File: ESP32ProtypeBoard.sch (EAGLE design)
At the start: 100 parts, among them IC1 SOIC-8, IC2 SI4431BDY, J10 POWER_JACKPTH_LOCK, Q2 MMBT3904, Q3 MMBT3904, U2 ESP-WROOM-32

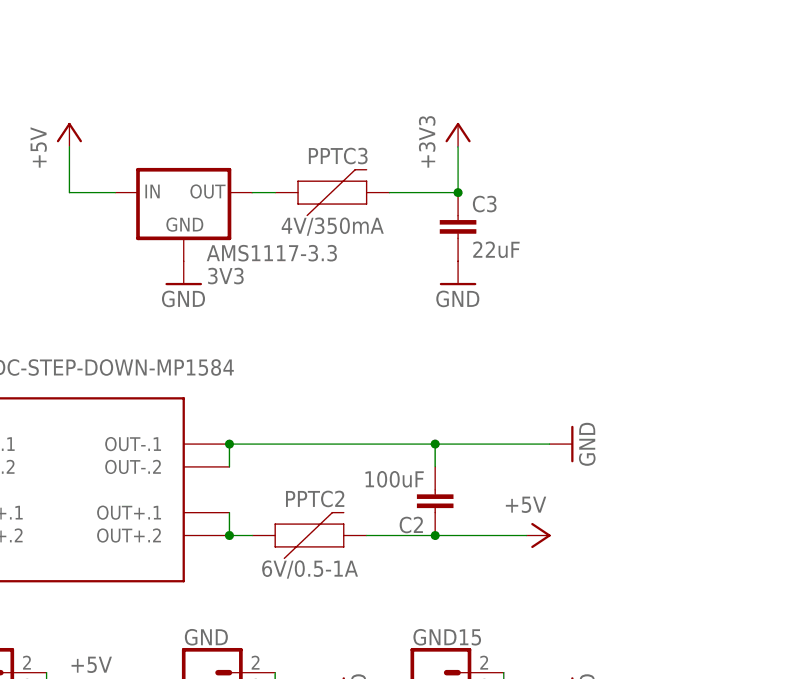
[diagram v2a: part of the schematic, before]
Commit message: Moved REG close to ESP to allow very small cutout
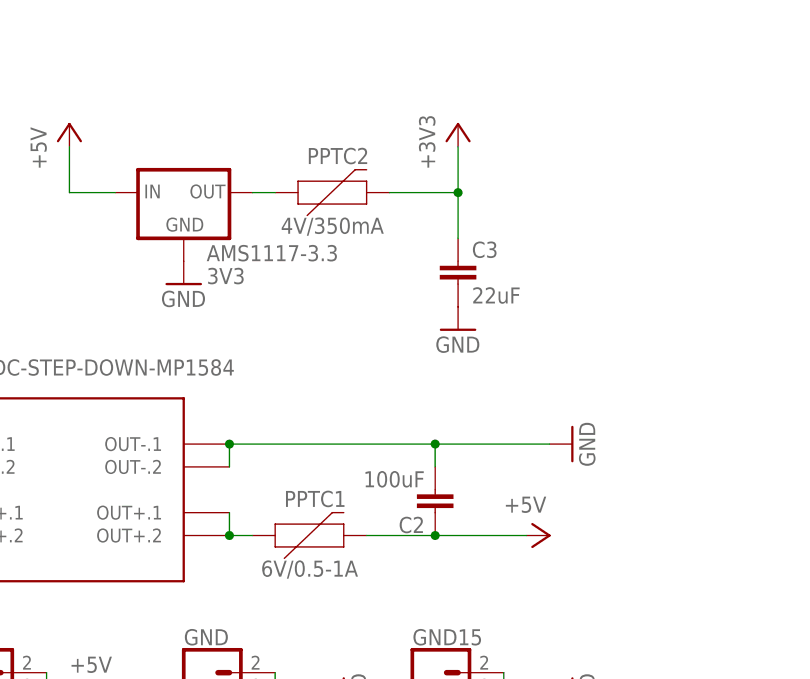
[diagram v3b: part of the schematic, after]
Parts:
- removed PPTC3: 4V/350mA, SparkFun-Fuses:PPTC_THREE-QUARTER-AMP
- added PPTC1: 6V/0.5-1A, SparkFun-Fuses:PPTC_THREE-QUARTER-AMP
- PPTC2: value 6V/0.5-1A -> 4V/350mA
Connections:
- net +3V3: now also PPTC2.2; no longer PPTC3.2
- net +5V: now also PPTC1.2; no longer PPTC2.2
- net 3V3OUT: now also PPTC2.1; no longer PPTC3.1
- net 5VOUT: now also PPTC1.1; no longer PPTC2.1
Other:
- moved on the sheet: C3, PPTC2
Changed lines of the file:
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@@
 <part name="+3V2" library="supply1" library_urn="urn:adsk.eagle:library:371" deviceset="+3V3" device=""/>
 <part name="P+11" library="supply1" library_urn="urn:adsk.eagle:library:371" deviceset="VCC" device=""/>
-<part name="PPTC2" library="SparkFun-Fuses" deviceset="PPTC" device="_THREE-QUARTER-AMP" value="6V/0.5-1A"/>
-<part name="PPTC3" library="SparkFun-Fuses" deviceset="PPTC" device="_THREE-QUARTER-AMP" value="4V/350mA"/>
+<part name="PPTC1" library="SparkFun-Fuses" deviceset="PPTC" device="_THREE-QUARTER-AMP" value="6V/0.5-1A"/>
+<part name="PPTC2" library="SparkFun-Fuses" deviceset="PPTC" device="_THREE-QUARTER-AMP" value="4V/350mA"/>
 <part name="+3V10" library="supply1" library_urn="urn:adsk.eagle:library:371" deviceset="+3V3" device=""/>
 <part name="GND4" library="supply1" library_urn="urn:adsk.eagle:library:371" deviceset="GND" device=""/>
@@
 <attribute name="VALUE" x="38.1" y="81.28" size="1.778" layer="96" rot="R90"/>
 </instance>
-<instance part="C3" gate="G$1" x="106.68" y="88.9" smashed="yes">
-<attribute name="NAME" x="108.204" y="89.281" size="1.778" layer="95"/>
-<attribute name="VALUE" x="108.204" y="84.201" size="1.778" layer="96"/>
-</instance>
-<instance part="GND13" gate="1" x="106.68" y="81.28" smashed="yes">
-<attribute name="VALUE" x="104.14" y="78.74" size="1.778" layer="96"/>
+<instance part="C3" gate="G$1" x="106.68" y="83.82" smashed="yes">
+<attribute name="NAME" x="108.204" y="84.201" size="1.778" layer="95"/>
+<attribute name="VALUE" x="108.204" y="79.121" size="1.778" layer="96"/>
+</instance>
+<instance part="GND13" gate="1" x="106.68" y="76.2" smashed="yes">
+<attribute name="VALUE" x="104.14" y="73.66" size="1.778" layer="96"/>
 </instance>
 <instance part="+5V" gate="G$1" x="53.34" y="35.56" smashed="yes">
@@
 <attribute name="VALUE" x="22.86" y="15.24" size="1.778" layer="96" rot="R180"/>
 </instance>
-<instance part="PPTC2" gate="F1" x="88.9" y="53.34" smashed="yes">
+<instance part="PPTC1" gate="F1" x="88.9" y="53.34" smashed="yes">
 <attribute name="NAME" x="90.805" y="56.515" size="1.778" layer="95" font="vector" align="bottom-center"/>
 <attribute name="VALUE" x="90.17" y="50.546" size="1.778" layer="96" font="vector" align="top-center"/>
 </instance>
-<instance part="PPTC3" gate="F1" x="91.44" y="91.44" smashed="yes">
+<instance part="PPTC2" gate="F1" x="91.44" y="91.44" smashed="yes">
 <attribute name="NAME" x="93.345" y="94.615" size="1.778" layer="95" font="vector" align="bottom-center"/>
 <attribute name="VALUE" x="92.71" y="88.646" size="1.778" layer="96" font="vector" align="top-center"/>
@@
 <segment>
 <pinref part="+3V4" gate="G$1" pin="+3V3"/>
+<wire x1="106.68" y1="91.44" x2="106.68" y2="96.52" width="0.1524" layer="91"/>
+<pinref part="PPTC2" gate="F1" pin="2"/>
+<wire x1="99.06" y1="91.44" x2="106.68" y2="91.44" width="0.1524" layer="91"/>
 <pinref part="C3" gate="G$1" pin="1"/>
-<wire x1="106.68" y1="91.44" x2="106.68" y2="96.52" width="0.1524" layer="91"/>
+<wire x1="106.68" y1="86.36" x2="106.68" y2="91.44" width="0.1524" layer="91"/>
 <junction x="106.68" y="91.44"/>
-<wire x1="99.06" y1="91.44" x2="106.68" y2="91.44" width="0.1524" layer="91"/>
-<pinref part="PPTC3" gate="F1" pin="2"/>
 </segment>
 <segment>
@@
 <pinref part="P+1" gate="1" pin="+5V"/>
 <wire x1="96.52" y1="53.34" x2="104.14" y2="53.34" width="0.1524" layer="91"/>
-<pinref part="PPTC2" gate="F1" pin="2"/>
+<pinref part="PPTC1" gate="F1" pin="2"/>
 </segment>
 <segment>
@@
 <net name="5VOUT" class="0">
 <segment>
-<pinref part="PPTC2" gate="F1" pin="1"/>
+<pinref part="PPTC1" gate="F1" pin="1"/>
 <pinref part="U$2" gate="G$1" pin="OUT+.2"/>
 <pinref part="U$2" gate="G$1" pin="OUT+.1"/>
@@
 <pinref part="AMS1117-3.3" gate="G$1" pin="OUT"/>
 <wire x1="83.82" y1="91.44" x2="86.36" y2="91.44" width="0.1524" layer="91"/>
-<pinref part="PPTC3" gate="F1" pin="1"/>
-</segment>
-</net>
+<pinref part="PPTC2" gate="F1" pin="1"/>
+</segment>
+</net>

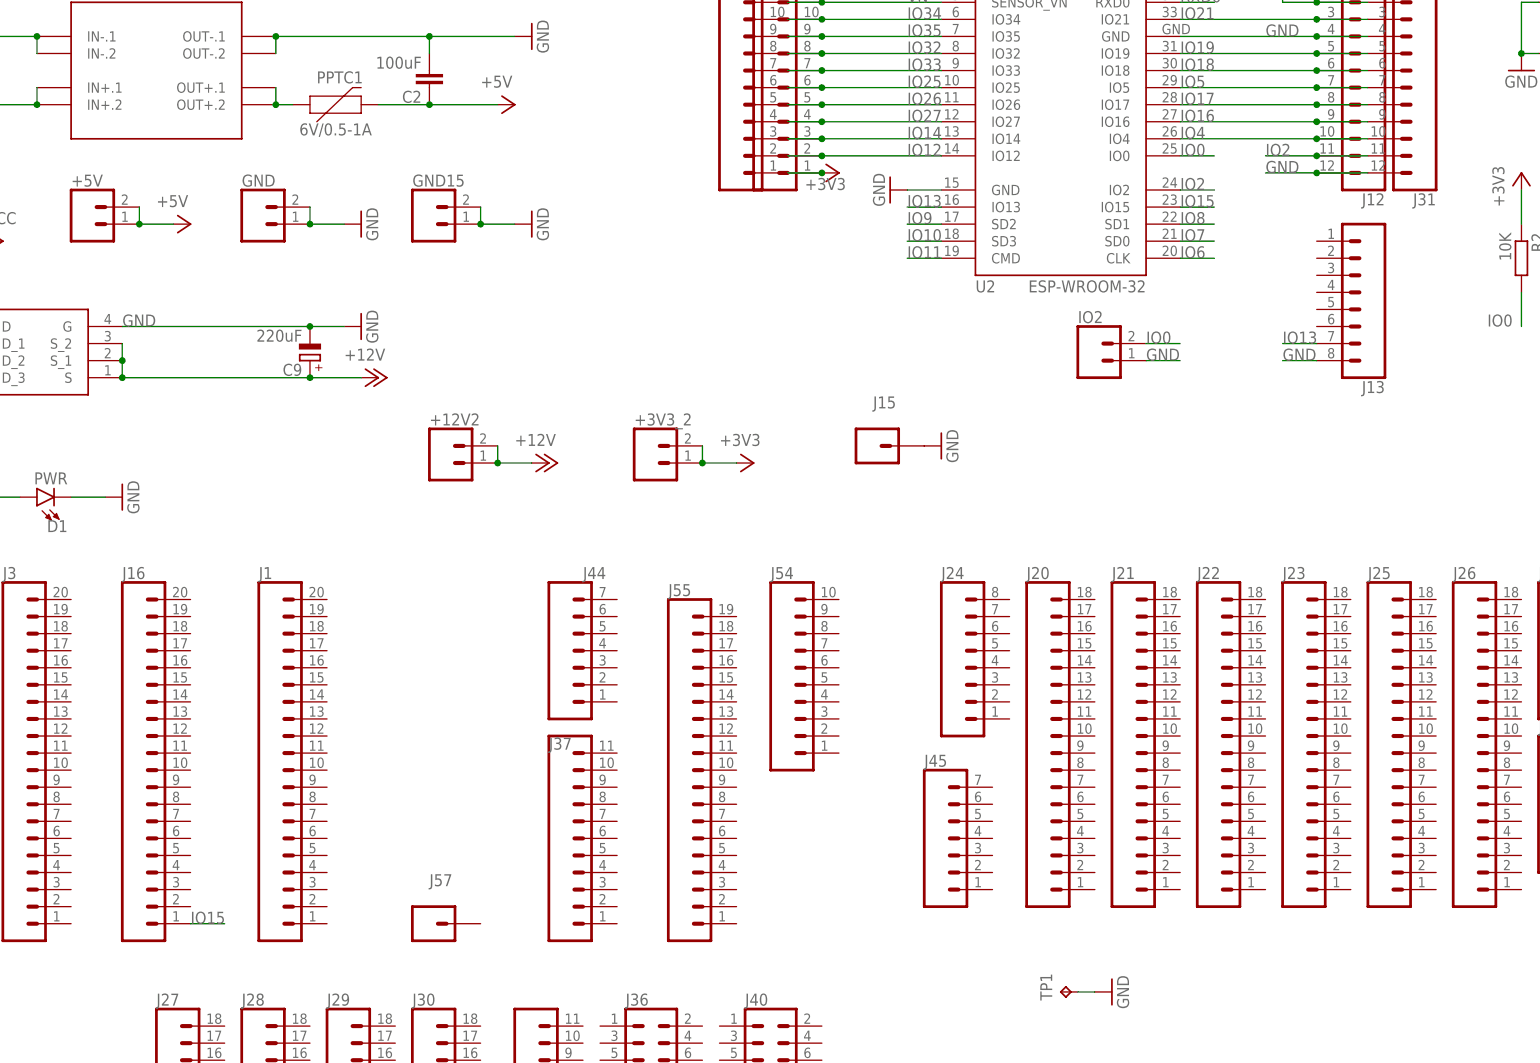
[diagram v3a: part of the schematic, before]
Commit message: Rewired pins under ESP etc
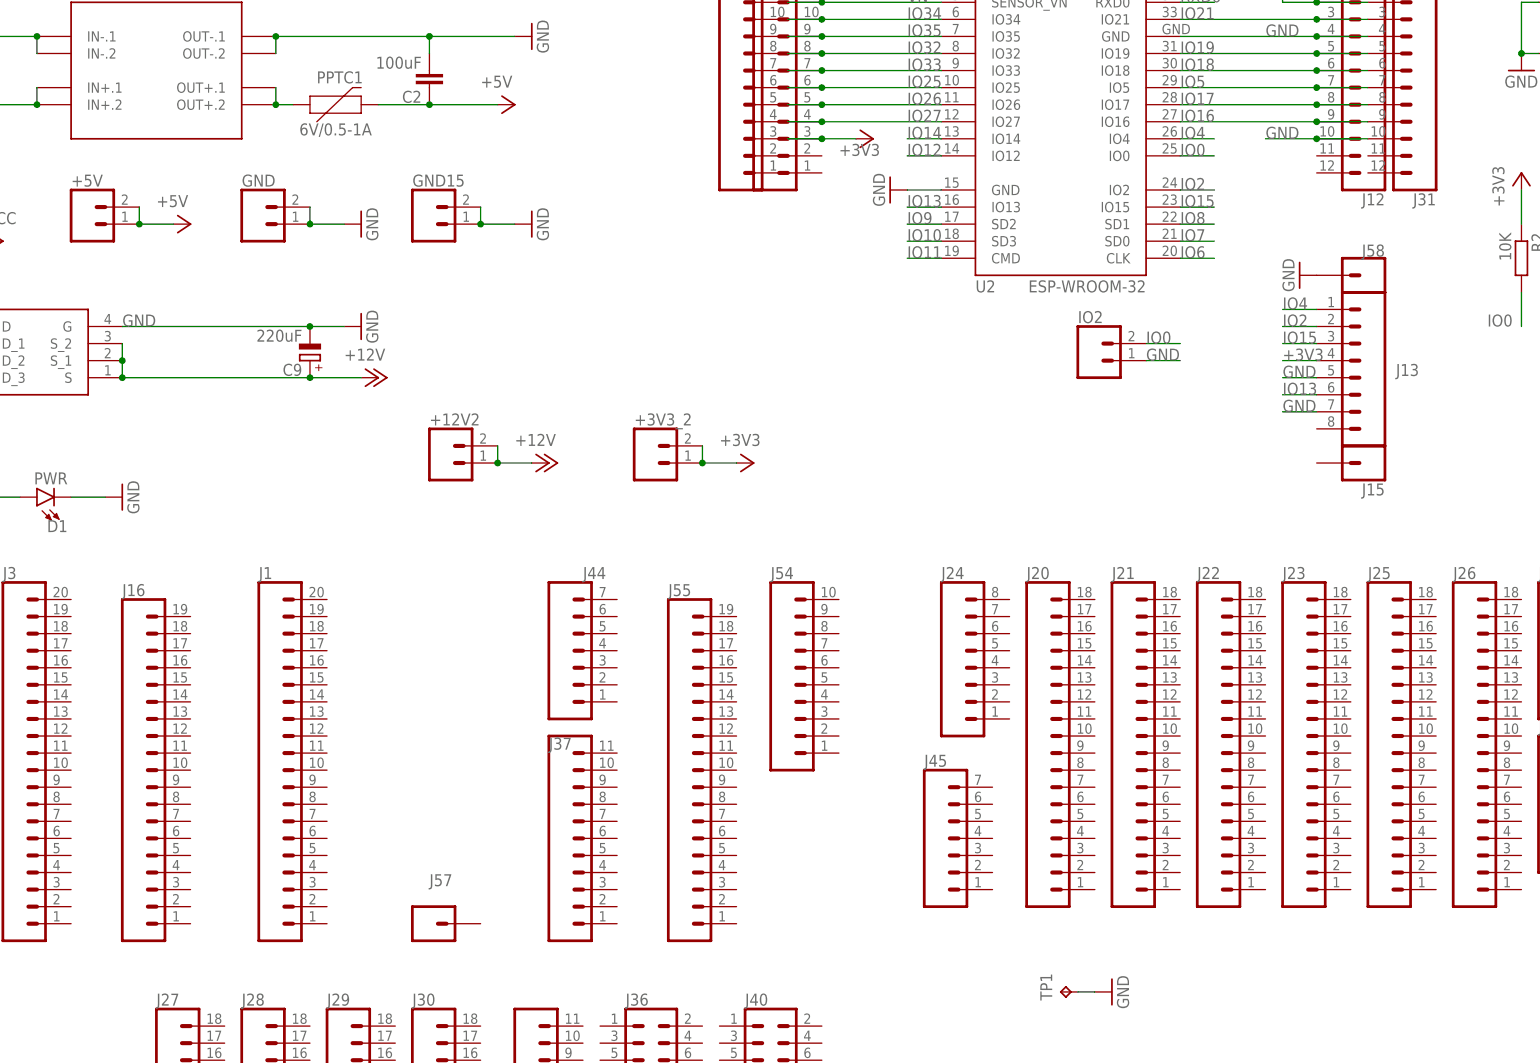
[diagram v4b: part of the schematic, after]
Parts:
- added J58: (no value), SparkFun-Connectors:CONN_01PTH_NO_SILK_KIT
- J16: device SparkFun-Connectors:CONN_20NOSILK -> SparkFun-Connectors:CONN_191X19_NO_SILK
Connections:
- net +3V3: now also J11.3, J13.4, J14.3; no longer J11.1, J14.1
- net GND: now also J12.10, J13.5, J13.7, J31.10, J58.1; no longer J12.12, J13.8, J15.1, J31.12
- net IO12: no longer J11.2, J14.2
- net IO13: now also J13.6; no longer J13.7
- net IO14: no longer J11.3, J14.3
- net IO15: now also J13.3; no longer J16.1
- net IO2: now also J13.2; no longer J12.11, J31.11
- net IO4: now also J13.1; no longer J12.10, J31.10
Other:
- moved on the sheet: J13, J15

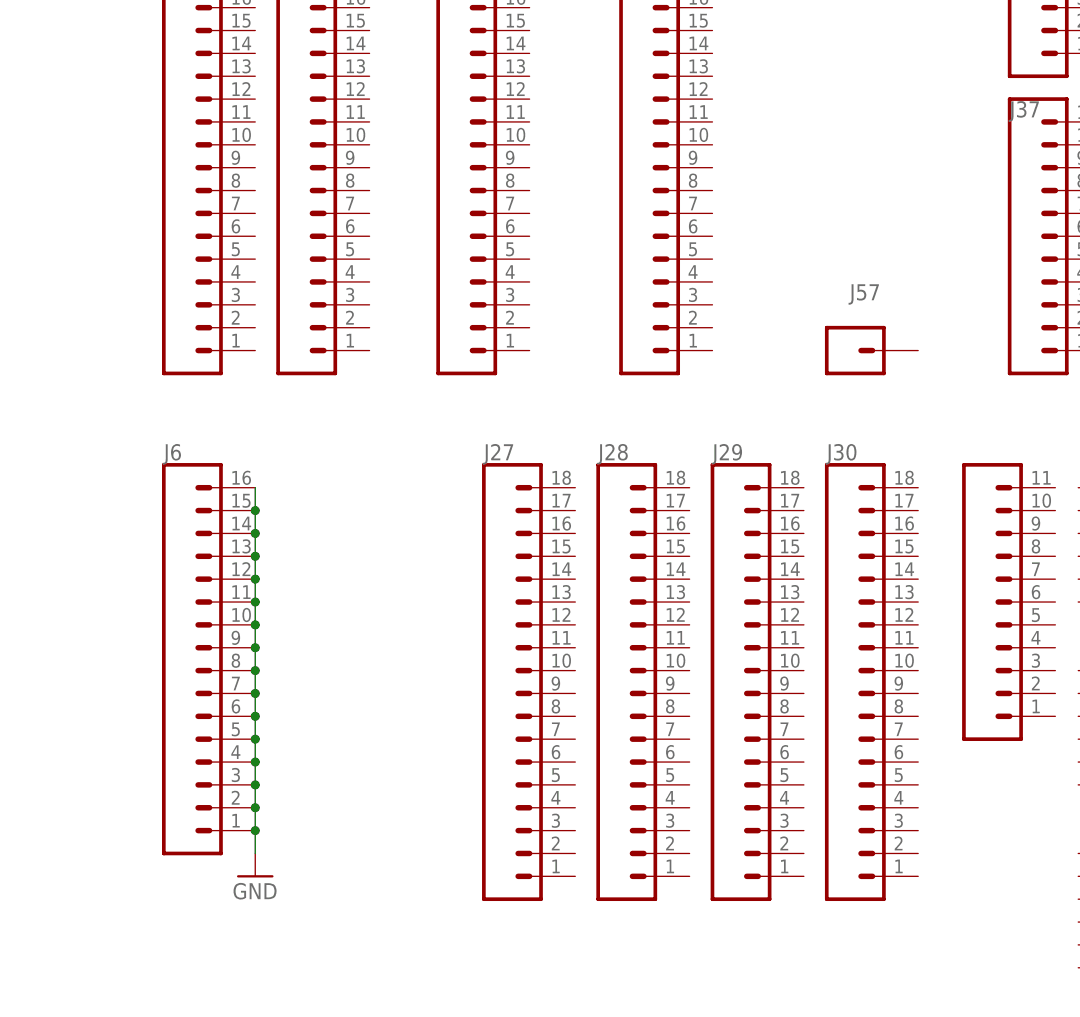
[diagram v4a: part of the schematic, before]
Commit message: Moving around power pins to save space
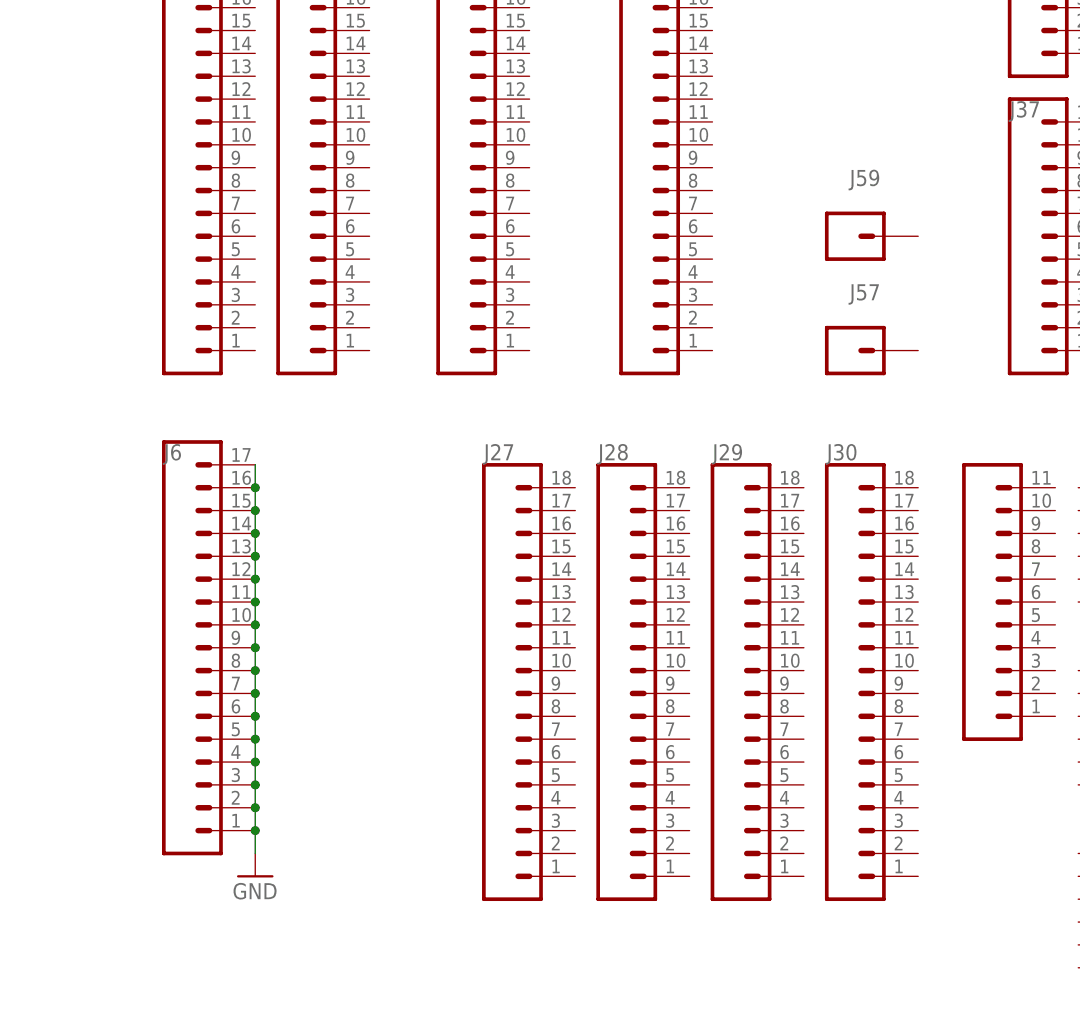
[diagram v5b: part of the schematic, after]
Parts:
- added J59: (no value), SparkFun-Connectors:CONN_01PTH_NO_SILK_KIT
- J6: device SparkFun-Connectors:CONN_161X16_NO_SILK -> SparkFun-Connectors:CONN_17NOSILK
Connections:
- net GND: now also J6.17
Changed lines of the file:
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@@
 <part name="J4" library="SparkFun-Connectors" library_urn="urn:adsk.eagle:library:513" deviceset="CONN_02" device="1X02_NO_SILK" package3d_urn="urn:adsk.eagle:package:38051/1"/>
 <part name="J5" library="SparkFun-Connectors" deviceset="CONN_16" device="1X16_NO_SILK"/>
-<part name="J6" library="SparkFun-Connectors" deviceset="CONN_16" device="1X16_NO_SILK"/>
+<part name="J6" library="SparkFun-Connectors" library_urn="urn:adsk.eagle:library:513" deviceset="CONN_17" device="NOSILK" package3d_urn="urn:adsk.eagle:package:38192/1"/>
 <part name="J7" library="SparkFun-Connectors" deviceset="CONN_06X2" device="NO_SILK"/>
 <part name="J8" library="SparkFun-Connectors" library_urn="urn:adsk.eagle:library:513" deviceset="CONN_11" device="1X11_NO_SILK" package3d_urn="urn:adsk.eagle:package:38260/1"/>
@@
 <part name="GND9" library="supply1" library_urn="urn:adsk.eagle:library:371" deviceset="GND" device=""/>
 <part name="+3V7" library="supply1" library_urn="urn:adsk.eagle:library:371" deviceset="+3V3" device=""/>
+<part name="J59" library="SparkFun-Connectors" library_urn="urn:adsk.eagle:library:513" deviceset="CONN_01" device="PTH_NO_SILK_KIT" package3d_urn="urn:adsk.eagle:package:38038/1"/>
 </parts>
 <sheets>
@@
 <instance part="+3V7" gate="G$1" x="170.18" y="48.26" smashed="yes" rot="R270">
 <attribute name="VALUE" x="165.1" y="45.72" size="1.778" layer="96"/>
+</instance>
+<instance part="J59" gate="G$1" x="104.14" y="-55.88" smashed="yes">
+<attribute name="VALUE" x="104.14" y="-55.626" size="1.778" layer="96" font="vector"/>
+<attribute name="NAME" x="104.14" y="-50.292" size="1.778" layer="95" font="vector"/>
 </instance>
 </instances>
@@
 <wire x1="38.1" y1="-86.36" x2="38.1" y2="-83.82" width="0.1524" layer="91"/>
 <junction x="38.1" y="-86.36"/>
-</segment>
-<segment>
+<pinref part="J6" gate="G$1" pin="17"/>
+<wire x1="38.1" y1="-81.28" x2="38.1" y2="-83.82" width="0.1524" layer="91"/>
+<junction x="38.1" y="-83.82"/>
+</segment>
+<segment>
